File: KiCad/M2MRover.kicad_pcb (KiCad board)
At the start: 2 copper layers, 80 x 90 mm, 22 parts, among them J1 Light Detection, J10 MPU6050 Gyro & Acc GY-521, J11 microbit_edge_connector, J2 Serial (Bluetooth), J3 Servo, J4 H-Bridge, J5 Ultrasonic Down, J6 Ultrasonic Forward, J7 Compass GY-273, J8 Left Hall, J9 Right Hall, U1 LM1117-3.3, U2 ESP8266-ESP-01

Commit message: Change 3.3V regulator to LD1117
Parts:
- U1: value LM1117-3.3 -> LD1117V33
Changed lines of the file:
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@@
     (add_net Ultrasonic_Forward_Trigger)
+  )
+  (module Package_TO_SOT_THT:TO-220-3_Vertical (layer F.Cu)
+    (at 181.61 93.98 90)
+    (descr "TO-220-3, Vertical, RM 2.54mm, see https://www.vishay.com/docs/66542/to-220-1.pdf")
+    (tags "TO-220-3 Vertical RM 2.54mm")
+    (fp_text reference U1 (at 2.54 -4.27 90) (layer F.SilkS)
+      (effects (font (size 1 1) (thickness 0.15)))
+    )
+    (fp_text value LD1117V33 (at 2.54 2.5 90) (layer F.Fab)
+      (effects (font (size 1 1) (thickness 0.15)))
+    )
+    (fp_text user %R (at 2.54 -4.27 90) (layer F.Fab)
+      (effects (font (size 1 1) (thickness 0.15)))
+    )
+    (fp_line (start 7.79 -3.4) (end -2.71 -3.4) (layer F.CrtYd) (width 0.05))
+    (fp_line (start 7.79 1.51) (end 7.79 -3.4) (layer F.CrtYd) (width 0.05))
+    (fp_line (start -2.71 1.51) (end 7.79 1.51) (layer F.CrtYd) (width 0.05))
+    (fp_line (start -2.71 -3.4) (end -2.71 1.51) (layer F.CrtYd) (width 0.05))
+    (fp_line (start 4.391 -3.27) (end 4.391 -1.76) (layer F.SilkS) (width 0.12))
+    (fp_line (start 0.69 -3.27) (end 0.69 -1.76) (layer F.SilkS) (width 0.12))
+    (fp_line (start -2.58 -1.76) (end 7.66 -1.76) (layer F.SilkS) (width 0.12))
+    (fp_line (start 7.66 -3.27) (end 7.66 1.371) (layer F.SilkS) (width 0.12))
+    (fp_line (start -2.58 -3.27) (end -2.58 1.371) (layer F.SilkS) (width 0.12))
+    (fp_line (start -2.58 1.371) (end 7.66 1.371) (layer F.SilkS) (width 0.12))
+    (fp_line (start -2.58 -3.27) (end 7.66 -3.27) (layer F.SilkS) (width 0.12))
+    (fp_line (start 4.39 -3.15) (end 4.39 -1.88) (layer F.Fab) (width 0.1))
+    (fp_line (start 0.69 -3.15) (end 0.69 -1.88) (layer F.Fab) (width 0.1))
+    (fp_line (start -2.46 -1.88) (end 7.54 -1.88) (layer F.Fab) (width 0.1))
+    (fp_line (start 7.54 -3.15) (end -2.46 -3.15) (layer F.Fab) (width 0.1))
+    (fp_line (start 7.54 1.25) (end 7.54 -3.15) (layer F.Fab) (width 0.1))
+    (fp_line (start -2.46 1.25) (end 7.54 1.25) (layer F.Fab) (width 0.1))
+    (fp_line (start -2.46 -3.15) (end -2.46 1.25) (layer F.Fab) (width 0.1))
+    (pad 3 thru_hole oval (at 5.08 0 90) (size 1.905 2) (drill 1.1) (layers *.Cu *.Mask)
+      (net 9 +5V))
+    (pad 2 thru_hole oval (at 2.54 0 90) (size 1.905 2) (drill 1.1) (layers *.Cu *.Mask)
+      (net 53 +3V3))
+    (pad 1 thru_hole rect (at 0 0 90) (size 1.905 2) (drill 1.1) (layers *.Cu *.Mask)
+      (net 5 GND))
+    (model ${KISYS3DMOD}/Package_TO_SOT_THT.3dshapes/TO-220-3_Vertical.wrl
+      (at (xyz 0 0 0))
+      (scale (xyz 1 1 1))
+      (rotate (xyz 0 0 0))
+    )
   )
   (module Connector_PinSocket_2.54mm:PinSocket_2x04_P2.54mm_Vertical (layer F.Cu)
@@
       (at (xyz 0 0 0))
       (scale (xyz 1 1 1))
-      (rotate (xyz 0 0 0))
-    )
-  )
-  (module Package_TO_SOT_THT:TO-220-3_Vertical (layer F.Cu)
-    (at 181.61 93.98 90)
-    (descr "TO-220-3, Vertical, RM 2.54mm, see https://www.vishay.com/docs/66542/to-220-1.pdf")
-    (tags "TO-220-3 Vertical RM 2.54mm")
-    (fp_text reference U1 (at 2.54 -4.27 90) (layer F.SilkS)
-      (effects (font (size 1 1) (thickness 0.15)))
-    )
-    (fp_text value LM1117-3.3 (at 2.54 2.5 90) (layer F.Fab)
-      (effects (font (size 1 1) (thickness 0.15)))
-    )
-    (fp_text user %R (at 2.54 -4.27 90) (layer F.Fab)
-      (effects (font (size 1 1) (thickness 0.15)))
-    )
-    (fp_line (start 7.79 -3.4) (end -2.71 -3.4) (layer F.CrtYd) (width 0.05))
-    (fp_line (start 7.79 1.51) (end 7.79 -3.4) (layer F.CrtYd) (width 0.05))
-    (fp_line (start -2.71 1.51) (end 7.79 1.51) (layer F.CrtYd) (width 0.05))
-    (fp_line (start -2.71 -3.4) (end -2.71 1.51) (layer F.CrtYd) (width 0.05))
-    (fp_line (start 4.391 -3.27) (end 4.391 -1.76) (layer F.SilkS) (width 0.12))
-    (fp_line (start 0.69 -3.27) (end 0.69 -1.76) (layer F.SilkS) (width 0.12))
-    (fp_line (start -2.58 -1.76) (end 7.66 -1.76) (layer F.SilkS) (width 0.12))
-    (fp_line (start 7.66 -3.27) (end 7.66 1.371) (layer F.SilkS) (width 0.12))
-    (fp_line (start -2.58 -3.27) (end -2.58 1.371) (layer F.SilkS) (width 0.12))
-    (fp_line (start -2.58 1.371) (end 7.66 1.371) (layer F.SilkS) (width 0.12))
-    (fp_line (start -2.58 -3.27) (end 7.66 -3.27) (layer F.SilkS) (width 0.12))
-    (fp_line (start 4.39 -3.15) (end 4.39 -1.88) (layer F.Fab) (width 0.1))
-    (fp_line (start 0.69 -3.15) (end 0.69 -1.88) (layer F.Fab) (width 0.1))
-    (fp_line (start -2.46 -1.88) (end 7.54 -1.88) (layer F.Fab) (width 0.1))
-    (fp_line (start 7.54 -3.15) (end -2.46 -3.15) (layer F.Fab) (width 0.1))
-    (fp_line (start 7.54 1.25) (end 7.54 -3.15) (layer F.Fab) (width 0.1))
-    (fp_line (start -2.46 1.25) (end 7.54 1.25) (layer F.Fab) (width 0.1))
-    (fp_line (start -2.46 -3.15) (end -2.46 1.25) (layer F.Fab) (width 0.1))
-    (pad 3 thru_hole oval (at 5.08 0 90) (size 1.905 2) (drill 1.1) (layers *.Cu *.Mask)
-      (net 9 +5V))
-    (pad 2 thru_hole oval (at 2.54 0 90) (size 1.905 2) (drill 1.1) (layers *.Cu *.Mask)
-      (net 53 +3V3))
-    (pad 1 thru_hole rect (at 0 0 90) (size 1.905 2) (drill 1.1) (layers *.Cu *.Mask)
-      (net 5 GND))
-    (model ${KISYS3DMOD}/Package_TO_SOT_THT.3dshapes/TO-220-3_Vertical.wrl
-      (at (xyz 0 0 0))
-      (scale (xyz 1 1 1))

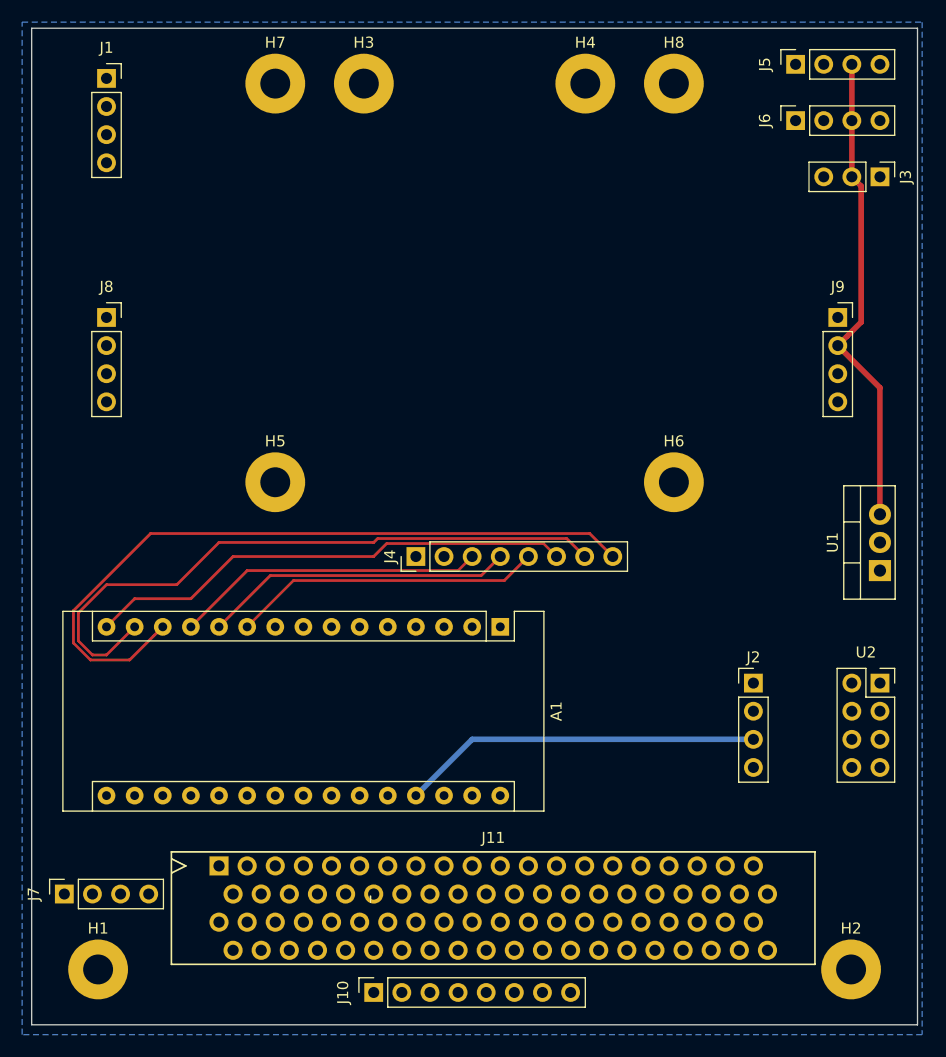
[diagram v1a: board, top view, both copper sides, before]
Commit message: Add passive components to PCB layout
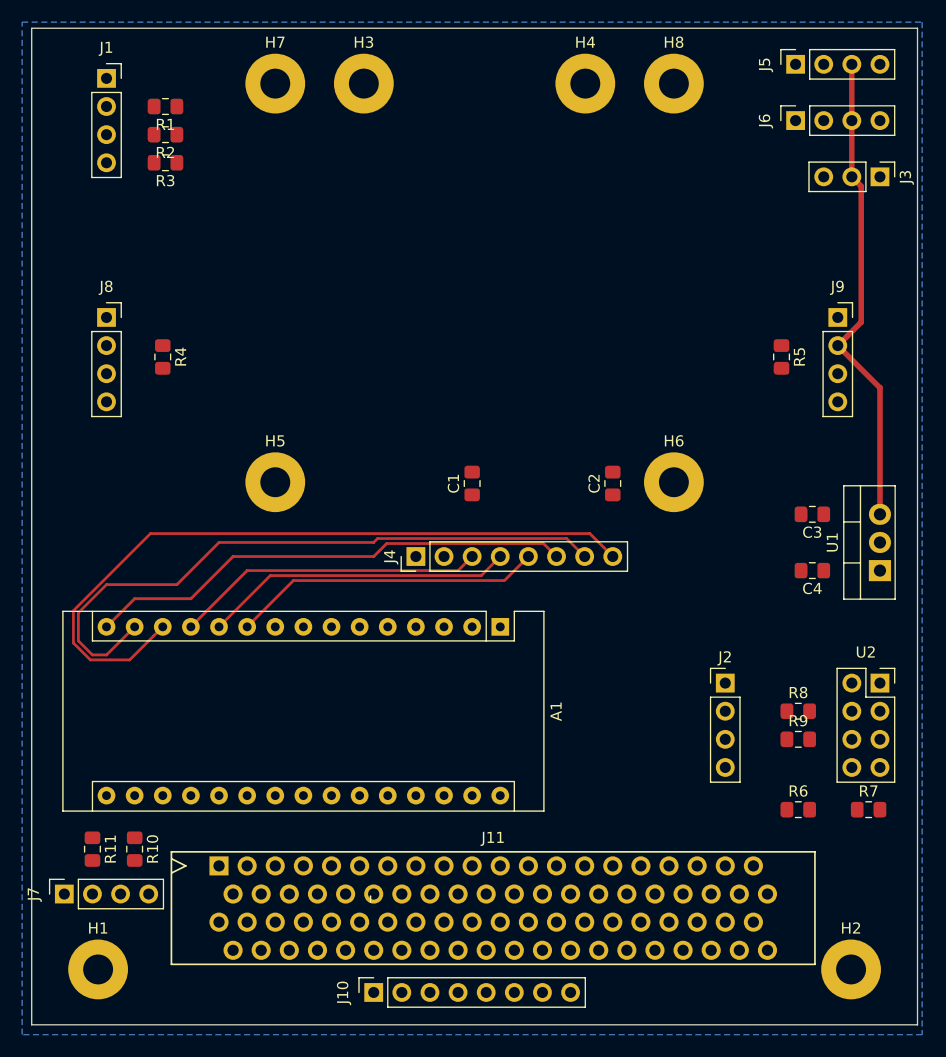
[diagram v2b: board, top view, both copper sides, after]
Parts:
- added C1: 10pF, Capacitor_SMD:C_0805_2012Metric_Pad1.15x1.40mm_HandSolder, F.Cu at (144.8, 86.1)
- added C2: 10pF, Capacitor_SMD:C_0805_2012Metric_Pad1.15x1.40mm_HandSolder, F.Cu at (157.5, 86.1)
- added C3: 100nF, Capacitor_SMD:C_0805_2012Metric_Pad1.15x1.40mm_HandSolder, F.Cu at (175.5, 88.9)
- added C4: 10uF, Capacitor_SMD:C_0805_2012Metric_Pad1.15x1.40mm_HandSolder, F.Cu at (175.5, 94.0)
- added R1: 10K, Resistor_SMD:R_0805_2012Metric_Pad1.15x1.40mm_HandSolder, F.Cu at (117.1, 52.1)
- added R10: 10K, Resistor_SMD:R_0805_2012Metric_Pad1.15x1.40mm_HandSolder, F.Cu at (114.3, 119.1)
- added R11: 10K, Resistor_SMD:R_0805_2012Metric_Pad1.15x1.40mm_HandSolder, F.Cu at (110.5, 119.1)
- added R2: 10K, Resistor_SMD:R_0805_2012Metric_Pad1.15x1.40mm_HandSolder, F.Cu at (117.1, 54.6)
- added R3: 10K, Resistor_SMD:R_0805_2012Metric_Pad1.15x1.40mm_HandSolder, F.Cu at (117.1, 57.1)
- added R4: 10K, Resistor_SMD:R_0805_2012Metric_Pad1.15x1.40mm_HandSolder, F.Cu at (116.8, 74.7)
- added R5: 10K, Resistor_SMD:R_0805_2012Metric_Pad1.15x1.40mm_HandSolder, F.Cu at (172.7, 74.7)
- added R6: 1K, Resistor_SMD:R_0805_2012Metric_Pad1.15x1.40mm_HandSolder, F.Cu at (174.2, 115.6)
- added R7: 2K, Resistor_SMD:R_0805_2012Metric_Pad1.15x1.40mm_HandSolder, F.Cu at (180.6, 115.6)
- added R8: 10K, Resistor_SMD:R_0805_2012Metric_Pad1.15x1.40mm_HandSolder, F.Cu at (174.2, 106.7)
- added R9: 10K, Resistor_SMD:R_0805_2012Metric_Pad1.15x1.40mm_HandSolder, F.Cu at (174.2, 109.2)
- moved J2 2.54 mm to (167.6, 104.1)
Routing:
- net +5V: track 76.0 -> 43.4 mm

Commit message: Add jumpers to I2C lines and start PCB layout
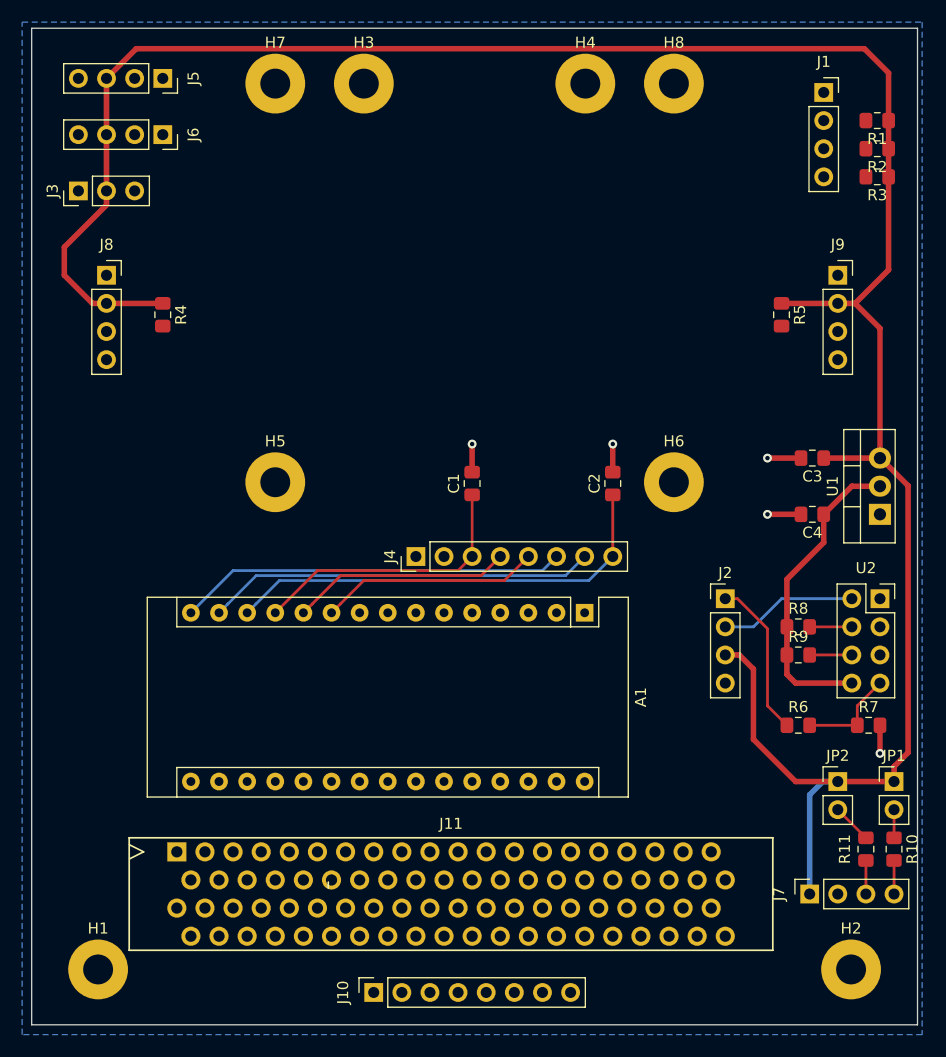
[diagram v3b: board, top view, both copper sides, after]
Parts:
- added JP1: Jumper_2_Open, Connector_PinHeader_2.54mm:PinHeader_1x02_P2.54mm_Vertical, F.Cu at (182.9, 113.0)
- added JP2: Jumper_2_Open, Connector_PinHeader_2.54mm:PinHeader_1x02_P2.54mm_Vertical, F.Cu at (177.8, 113.0)
- R10, R11: value 10K -> 4.7K
- moved J3 72.4 mm to (109.2, 59.7), turned to 90 degrees
- moved R11 69.9 mm to (180.3, 119.1)
- moved R10 68.6 mm to (182.9, 119.1)
- moved J7 67.3 mm to (175.3, 123.2)
- moved J1 64.8 mm to (176.5, 50.8)
- moved R1 64.3 mm to (181.4, 53.3)
- moved R2 64.3 mm to (181.4, 55.9)
- moved R3 64.3 mm to (181.4, 58.4)
- moved J5 57.2 mm to (116.8, 49.5), turned to 270 degrees
- moved J6 57.2 mm to (116.8, 54.6), turned to 270 degrees
- moved A1 7.73 mm to (154.9, 97.8)
- moved J2 7.62 mm to (167.6, 96.5)
- moved R8 7.62 mm to (174.2, 99.1)
- moved R9 7.62 mm to (174.2, 101.6)
- moved U2 7.62 mm to (181.6, 96.5)
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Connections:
- R10 pad 1: +5V -> Net-(JP1-Pad2)
- R11 pad 1: +5V -> Net-(JP2-Pad2)
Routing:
- net +5V: track 43.4 -> 217.1 mm
- net +3V3: track 0.00 -> 28.2 mm
- net ENB: track 65.3 -> 40.7 mm
- net IN4: track 58.4 -> 35.1 mm
- net TX: track 0.00 -> 14.4 mm
- net GND: track 0.00 -> 13.7 mm, vias 0 -> 5
- net RX: track 0.00 -> 12.5 mm
- net IN3: track 44.2 -> 35.1 mm
- net Net-(R6-Pad2): track 0.00 -> 8.96 mm
- net IN2: track 28.0 -> 19.9 mm
- net IN1: track 28.0 -> 19.9 mm
- net Net-(R9-Pad2): track 0.00 -> 3.81 mm
- net Net-(R8-Pad2): track 0.00 -> 3.81 mm
- net Net-(JP2-Pad2): track 0.00 -> 3.59 mm
- net SDA: track 0.00 -> 3.03 mm
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
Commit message: Add L298N H-Bridge driver
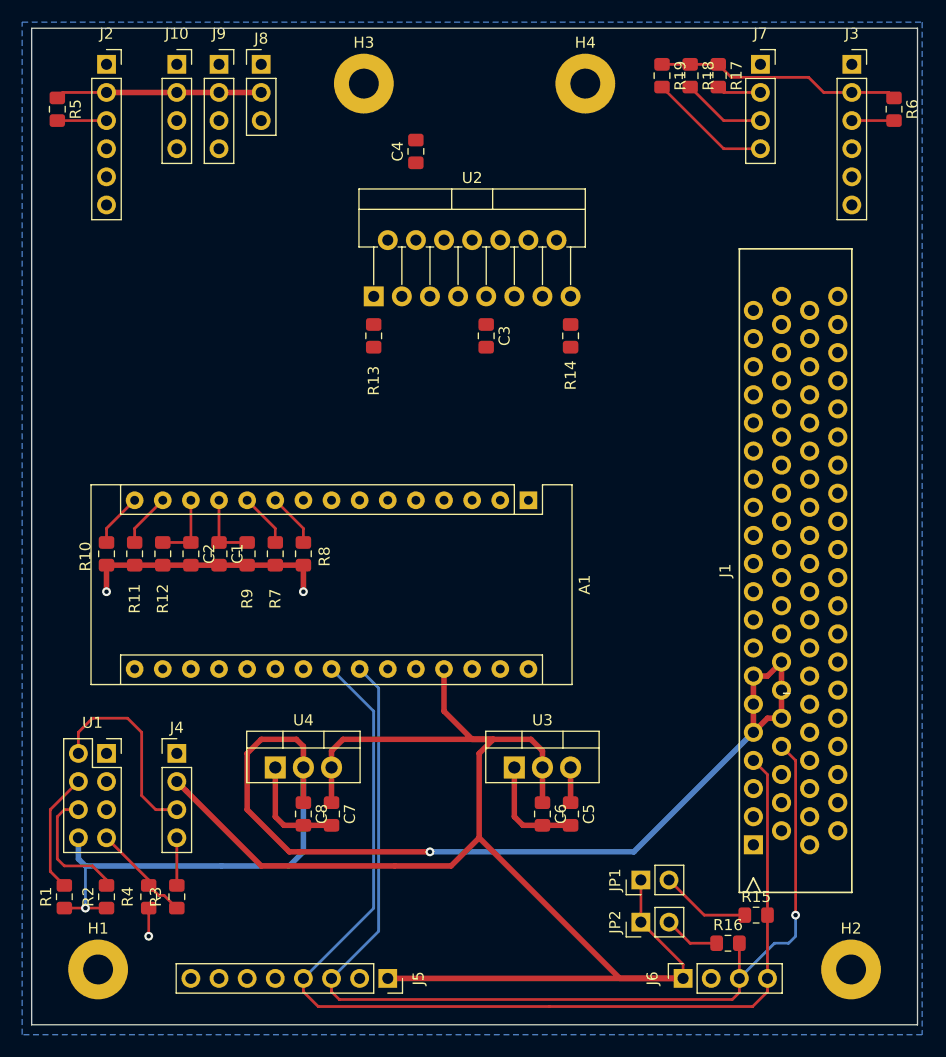
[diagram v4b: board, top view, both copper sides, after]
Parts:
- removed H5, H6, H7, H8: H-Bridge MountingHole, MountingHole:MountingHole_2.7mm_Pad
- removed J11: microbit_edge_connector, MCU_Module_Microbit:4UCON_17909_02x401.27mm_Vertical
- added C5: 100nF, Capacitor_SMD:C_0805_2012Metric_Pad1.15x1.40mm_HandSolder, F.Cu at (153.7, 116.0)
- added C6: 10uF, Capacitor_SMD:C_0805_2012Metric_Pad1.15x1.40mm_HandSolder, F.Cu at (151.1, 116.0)
- added C7: 100nF, Capacitor_SMD:C_0805_2012Metric_Pad1.15x1.40mm_HandSolder, F.Cu at (132.1, 116.0)
- added C8: 10uF, Capacitor_SMD:C_0805_2012Metric_Pad1.15x1.40mm_HandSolder, F.Cu at (129.5, 116.0)
- added R12: 10K, Resistor_SMD:R_0805_2012Metric_Pad1.15x1.40mm_HandSolder, F.Cu at (116.8, 92.5)
- added R13: 1R, Resistor_SMD:R_0805_2012Metric_Pad1.15x1.40mm_HandSolder, F.Cu at (135.9, 72.8)
- added R14: 1R, Resistor_SMD:R_0805_2012Metric_Pad1.15x1.40mm_HandSolder, F.Cu at (153.7, 72.8)
- added R15: 4.7K, Resistor_SMD:R_0805_2012Metric_Pad1.15x1.40mm_HandSolder, F.Cu at (170.4, 125.1)
- added R16: 4.7K, Resistor_SMD:R_0805_2012Metric_Pad1.15x1.40mm_HandSolder, F.Cu at (167.9, 127.6)
- added R17: 10K, Resistor_SMD:R_0805_2012Metric_Pad1.15x1.40mm_HandSolder, F.Cu at (167.0, 49.3)
- added R18: 10K, Resistor_SMD:R_0805_2012Metric_Pad1.15x1.40mm_HandSolder, F.Cu at (164.5, 49.3)
- added R19: 10K, Resistor_SMD:R_0805_2012Metric_Pad1.15x1.40mm_HandSolder, F.Cu at (161.9, 49.3)
- added U3: LD1117V50, Package_TO_SOT_THT:TO-220-3_Vertical, F.Cu at (148.6, 111.8)
- added U4: LD1117V33, Package_TO_SOT_THT:TO-220-3_Vertical, F.Cu at (127.0, 111.8)
- C4: value 10uF -> 100nF
- J1: value Light Detection -> microbit_edge_connector; footprint Connector_PinSocket_2.54mm:PinSocket_1x04_P2.54mm_Vertical -> MCU_Module_Microbit:4UCON_17909_02x401.27mm_Vertical
- J10: value MPU6050 Gyro & Acc GY-521 -> Ultrasonic Forward; footprint Connector_PinSocket_2.54mm:PinSocket_1x08_P2.54mm_Vertical -> Connector_PinSocket_2.54mm:PinSocket_1x04_P2.54mm_Vertical
- J2: value Serial (Bluetooth) -> Left Motor; footprint Connector_PinHeader_2.54mm:PinHeader_1x04_P2.54mm_Vertical -> Connector_PinSocket_2.54mm:PinSocket_1x06_P2.54mm_Vertical
- J3: value Servo -> Right Motor; footprint Connector_PinHeader_2.54mm:PinHeader_1x03_P2.54mm_Vertical -> Connector_PinSocket_2.54mm:PinSocket_1x06_P2.54mm_Vertical
- J4: value H-Bridge -> Serial (Bluetooth); footprint Connector_PinHeader_2.54mm:PinHeader_1x08_P2.54mm_Vertical -> Connector_PinHeader_2.54mm:PinHeader_1x04_P2.54mm_Vertical
- J5: value Ultrasonic Down -> MPU6050 Gyro & Acc GY-521; footprint Connector_PinSocket_2.54mm:PinSocket_1x04_P2.54mm_Vertical -> Connector_PinSocket_2.54mm:PinSocket_1x08_P2.54mm_Vertical
- J6: value Ultrasonic Forward -> Compass GY-273
- J7: value Compass GY-273 -> Light Detection
- J8: value Left Hall -> Servo; footprint Connector_PinSocket_2.54mm:PinSocket_1x04_P2.54mm_Vertical -> Connector_PinHeader_2.54mm:PinHeader_1x03_P2.54mm_Vertical
- J9: value Right Hall -> Ultrasonic Down
- R10, R11: value 4.7K -> 10K
- R3: value 10K -> 1K
- R4: value 10K -> 2K
- R6: value 1K -> 10K
- R7: value 2K -> 10K
- U1: value LD1117V33 -> ESP8266-ESP-01; footprint Package_TO_SOT_THT:TO-220-3_Vertical -> Connector_PinSocket_2.54mm:PinSocket_2x04_P2.54mm_Vertical
- U2: value ESP8266-ESP-01 -> L298HN; footprint Connector_PinSocket_2.54mm:PinSocket_2x04_P2.54mm_Vertical -> Package_TO_SOT_THT:TO-220-15_P2.54x2.54mm_StaggerOdd_Lead4.58mm_Vertical
- moved R1 101.5 mm to (108.0, 123.4), turned to 90 degrees
- moved R2 97.0 mm to (111.8, 123.4), turned to 90 degrees
- moved R3 90.7 mm to (118.1, 123.4), turned to 270 degrees
- moved J6 89.5 mm to (163.8, 130.8), turned to 90 degrees
- moved J10 85.7 mm to (118.1, 48.3), turned to 0 degrees
- moved J5 83.8 mm to (137.2, 130.8)
- moved R10 76.0 mm to (111.8, 92.5)
- moved J7 75.1 mm to (170.8, 48.3), turned to 0 degrees
- moved J2 73.8 mm to (111.8, 48.3)
- moved U1 73.1 mm to (111.8, 110.5), turned to 0 degrees
- moved R11 71.2 mm to (114.3, 92.5)
- moved J3 70.8 mm to (179.1, 48.3), turned to 0 degrees
- moved J1 68.2 mm to (170.2, 118.7), turned to 90 degrees
- moved R5 68.0 mm to (107.3, 52.3)
- moved J9 59.0 mm to (121.9, 48.3)
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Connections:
- C4 pad 1: +3V3 -> +BATT
- J1 pad 2: Right_LDR -> Net-(J1-Pad2)
- J1 pad 3: Middle_LDR -> GND
- J1 pad 4: Left_LDR -> Net-(J1-Pad4)
- J10 pad 1: +5V -> GND
- J10 pad 2: GND -> +5V
- J10 pad 3: SCL -> Ultrasonic_Forward_Echo
- J10 pad 4: SDA -> Ultrasonic_Forward_Trigger
- J2 pad 1: TX -> GND
- J2 pad 2: RX -> +5V
- J2 pad 3: +5V -> Left_Hall
- J2 pad 4: GND -> Left_LED
- J3 pad 3: Servo -> Right_Hall
- J4 pad 3: ENA -> RX
- J4 pad 4: IN1 -> TX
- J5 pad 1: Ultrasonic_Down_Trigger -> +5V
- J5 pad 2: Ultrasonic_Down_Echo -> GND
- J5 pad 3: +5V -> SCL
- J5 pad 4: GND -> SDA
- J6 pad 1: Ultrasonic_Forward_Trigger -> +5V
- J6 pad 2: Ultrasonic_Forward_Echo -> GND
- J6 pad 3: +5V -> SCL
- J6 pad 4: GND -> SDA
- J7 pad 1: +5V -> GND
- J7 pad 2: GND -> Right_LDR
- J7 pad 3: SCL -> Middle_LDR
- J7 pad 4: SDA -> Left_LDR
- J8 pad 3: Left_Hall -> Servo
- J9 pad 3: Right_Hall -> Ultrasonic_Down_Echo
- J9 pad 4: Right_LED -> Ultrasonic_Down_Trigger
- R1 pad 1: +5V -> +3V3
- R1 pad 2: Right_LDR -> Net-(R1-Pad2)
- R10 pad 1: Net-(JP1-Pad2) -> IN3
- R10 pad 2: SDA -> GND
- R11 pad 1: Net-(JP2-Pad2) -> IN4
- R11 pad 2: SCL -> GND
- R2 pad 1: +5V -> +3V3
- R2 pad 2: Middle_LDR -> Net-(R2-Pad2)
- R3 pad 1: +5V -> TX
- R3 pad 2: Left_LDR -> Net-(R3-Pad2)
- R4 pad 1: +5V -> Net-(R3-Pad2)
- R4 pad 2: Left_Hall -> GND
- R5 pad 2: Right_Hall -> Left_Hall
- R6 pad 1: TX -> +5V
- R6 pad 2: Net-(R6-Pad2) -> Right_Hall
- R7 pad 1: Net-(R6-Pad2) -> IN1
- R8 pad 1: +3V3 -> IN2
- R8 pad 2: Net-(R8-Pad2) -> GND
- R9 pad 1: +3V3 -> ENA
- R9 pad 2: Net-(R9-Pad2) -> GND
- U1 pad 2: +3V3 -> RX
- U1 pad 3: +5V -> Net-(U1-Pad3)
- U2 pad 1: GND -> Net-(R13-Pad1)
- U2 pad 2: RX -> OUT1
- U2 pad 3: Net-(U2-Pad3) -> OUT2
- U2 pad 4: Net-(R8-Pad2) -> +BATT
- U2 pad 5: Net-(U2-Pad5) -> IN1
- U2 pad 6: Net-(R9-Pad2) -> ENA
- U2 pad 7: Net-(R6-Pad2) -> IN2
- U2 pad 8: +3V3 -> GND
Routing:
- net SDA: track 3.03 -> 97.8 mm
- net SCL: track 3.03 -> 97.8 mm, vias 0 -> 1
- net +3V3: track 28.2 -> 122.3 mm, vias 0 -> 2
- net +5V: track 217.1 -> 181.1 mm
- net ENB: track 40.7 -> 6.35 mm
- net GND: track 13.7 -> 44.8 mm, vias 5 -> 3
- net IN3: track 35.1 -> 4.86 mm
- net IN4: track 35.1 -> 4.86 mm
- net ENA: track 25.5 -> 6.35 mm
- net IN2: track 19.9 -> 4.86 mm
- net IN1: track 19.9 -> 4.86 mm
- net Net-(R2-Pad2): track 0.00 -> 11.7 mm
- net Left_LDR: track 0.00 -> 11.2 mm
- net Net-(R1-Pad2): track 0.00 -> 11.0 mm
- net TX: track 14.4 -> 4.30 mm
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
